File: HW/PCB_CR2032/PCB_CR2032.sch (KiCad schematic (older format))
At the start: 0 parts

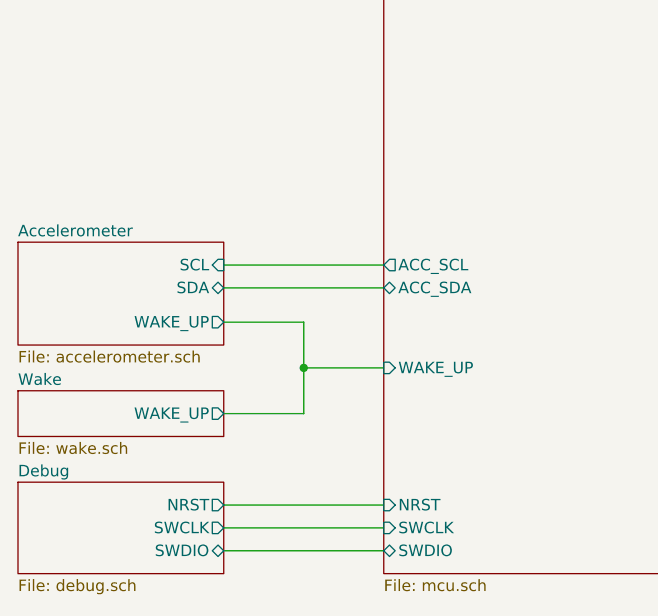
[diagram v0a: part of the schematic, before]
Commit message: * Updated Schematic with 1206 leds and 1k 0805 current limiting resistors
* Restored STDC14 and debug UART, now shared with top led of minute and second. Some other LED pins remapped

* Updated STM32CubeMX project to reflect schematic changes and generated code again
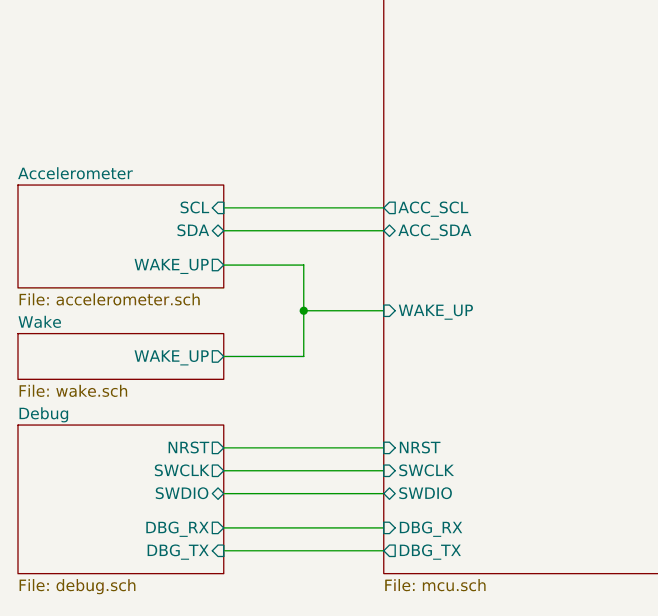
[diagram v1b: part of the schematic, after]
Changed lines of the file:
@@
 Sheet 1 7
 Title "BCD Watch"
-Date "2019-11-06"
-Rev "0.1"
+Date "2019-11-08"
+Rev "0.3"
 Comp ""
 Comment1 ""
@@
 $EndSheet
 $Sheet
-S 2550 4850 900  400
+S 2550 4600 900  650
 U 5DD47181
 F0 "Debug" 50
 F1 "debug.sch" 50
-F2 "NRST" O R 3450 4950 50
-F3 "SWCLK" O R 3450 5050 50
-F4 "SWDIO" B R 3450 5150 50
-$EndSheet
-$Sheet
-S 2550 4450 900  200
+F2 "NRST" O R 3450 4700 50
+F3 "SWCLK" O R 3450 4800 50
+F4 "SWDIO" B R 3450 4900 50
+F5 "DBG_RX" O R 3450 5050 50
+F6 "DBG_TX" I R 3450 5150 50
+$EndSheet
+$Sheet
+S 2550 4200 900  200
 U 5DD502F6
 F0 "Wake" 50
 F1 "wake.sch" 50
-F2 "WAKE_UP" O R 3450 4550 50
-$EndSheet
-Wire Wire Line
-	3450 4950 4150 4950
-Wire Wire Line
-	3450 5050 4150 5050
-Wire Wire Line
-	3450 5150 4150 5150
-$Sheet
-S 2550 3800 900  450
+F2 "WAKE_UP" O R 3450 4300 50
+$EndSheet
+$Sheet
+S 2550 3550 900  450
 U 5DC486A4
 F0 "Accelerometer" 50
 F1 "accelerometer.sch" 50
-F2 "SCL" I R 3450 3900 50
-F3 "SDA" B R 3450 4000 50
-F4 "WAKE_UP" O R 3450 4150 50
-$EndSheet
-Wire Wire Line
-	3450 4150 3800 4150
-Wire Wire Line
-	3800 4150 3800 4350
-Wire Wire Line
-	3800 4350 4150 4350
-Wire Wire Line
-	3450 4550 3800 4550
-Wire Wire Line
-	3800 4550 3800 4350
-Connection ~ 3800 4350
+F2 "SCL" I R 3450 3650 50
+F3 "SDA" B R 3450 3750 50
+F4 "WAKE_UP" O R 3450 3900 50
+$EndSheet
+Wire Wire Line
+	3450 3900 3800 3900
+Wire Wire Line
+	3800 3900 3800 4100
+Wire Wire Line
+	3800 4100 4150 4100
+Wire Wire Line
+	3450 4300 3800 4300
+Wire Wire Line
+	3800 4300 3800 4100
+Connection ~ 3800 4100
 $Sheet
 S 2550 2000 900  400
@@
 F20 "LED_S_01" O R 6400 4250 50
 F21 "LED_S_00" O R 6400 4350 50
-F22 "SWCLK" I L 4150 5050 50
-F23 "SWDIO" B L 4150 5150 50
-F24 "NRST" I L 4150 4950 50
-F25 "WAKE_UP" I L 4150 4350 50
+F22 "SWCLK" I L 4150 4800 50
+F23 "SWDIO" B L 4150 4900 50
+F24 "NRST" I L 4150 4700 50
+F25 "WAKE_UP" I L 4150 4100 50
 F26 "LED_H_1_DIM" O R 6400 4550 50
 F27 "LED_H_0_DIM" O R 6400 4650 50
@@
 F34 "LED_M_13" O R 6400 2650 50
 F35 "LED_S_13" O R 6400 3600 50
-F36 "ACC_SDA" B L 4150 4000 50
-F37 "ACC_SCL" O L 4150 3900 50
-$EndSheet
-Wire Wire Line
-	3450 3900 4150 3900
-Wire Wire Line
-	3450 4000 4150 4000
+F36 "ACC_SDA" B L 4150 3750 50
+F37 "ACC_SCL" O L 4150 3650 50
+F38 "DBG_TX" O L 4150 5150 50
+F39 "DBG_RX" I L 4150 5050 50
+$EndSheet
+Wire Wire Line
+	3450 3650 4150 3650
+Wire Wire Line
+	3450 3750 4150 3750
 Wire Wire Line
 	6400 5150 7100 5150
@@
 Wire Wire Line
 	6400 1700 7100 1700
+Wire Wire Line
+	4150 4700 3450 4700
+Wire Wire Line
+	3450 4800 4150 4800
+Wire Wire Line
+	3450 4900 4150 4900
+Wire Wire Line
+	3450 5050 4150 5050
+Wire Wire Line
+	3450 5150 4150 5150
 $EndSCHEMATC

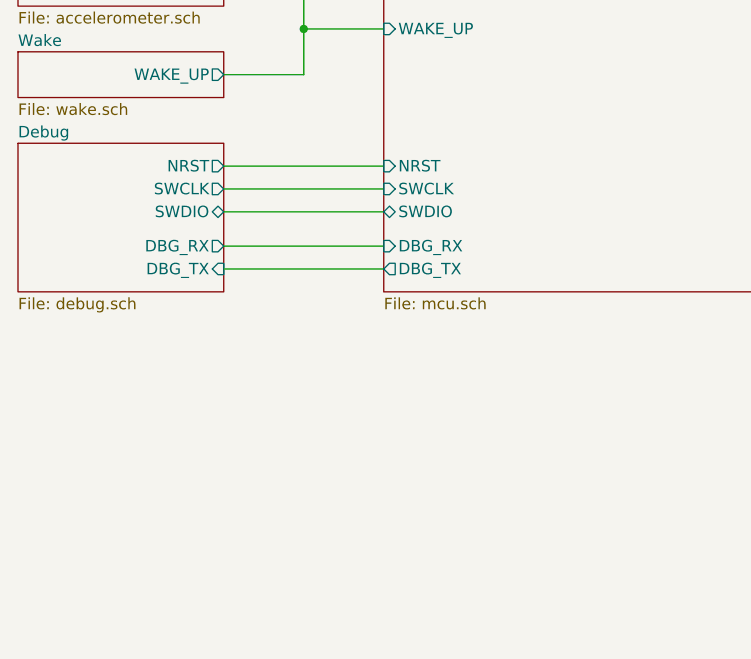
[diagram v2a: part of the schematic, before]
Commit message: Worked on Rev 2.0 HW with smaller size.
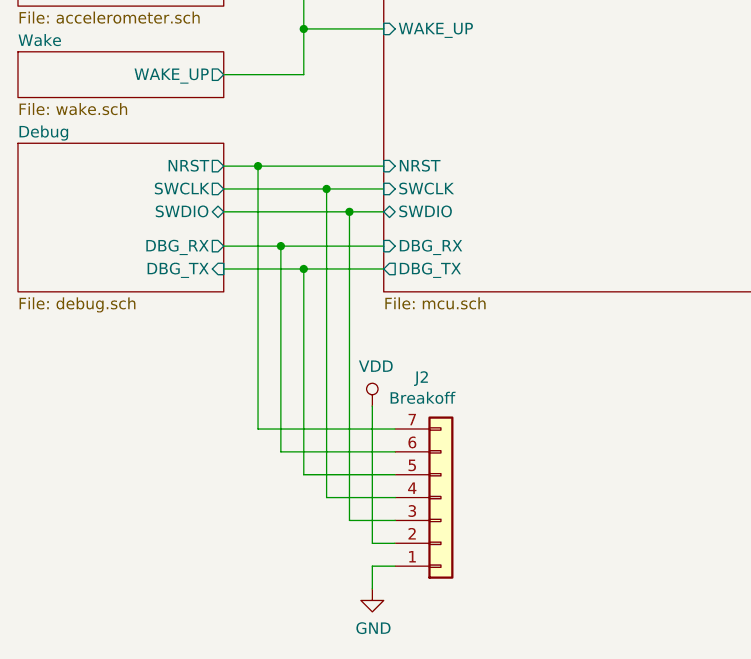
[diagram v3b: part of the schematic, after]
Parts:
- added J2: Breakoff, Connector_PinHeader_1.27mm:PinHeader_1x07_P1.27mm_Vertical, symbol Connector_Generic:Conn_01x07
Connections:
- net Debug/DBG_RX: now also J2.6 (Pin_6)
- net Debug/DBG_TX: now also J2.5 (Pin_5)
- net Debug/NRST: now also J2.7 (Pin_7)
- net Debug/SWCLK: now also J2.4 (Pin_4)
- net Debug/SWDIO: now also J2.3 (Pin_3)
- new net GND: J2.1 (Pin_1)
- new net VDD: J2.2 (Pin_2)
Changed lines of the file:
@@
 Wire Wire Line
 	6400 1700 7100 1700
+$Comp
+L Connector_Generic:Conn_01x07 J2
+U 1 1 5DCC8438
+P 4400 6150
+F 0 "J2" H 4318 5625 50  0000 C CNN
+F 1 "Breakoff" H 4318 5716 50  0000 C CNN
+F 2 "Connector_PinHeader_1.27mm:PinHeader_1x07_P1.27mm_Vertical" H 4400 6150 50  0001 C CNN
+F 3 "~" H 4400 6150 50  0001 C CNN
+	1    4400 6150
+	1    0    0    1
+$EndComp
+$Comp
+L power:GND #PWR017
+U 1 1 5DCCDE70
+P 4100 6550
+F 0 "#PWR017" H 4100 6300 50  0001 C CNN
+F 1 "GND" H 4105 6377 50  0000 C CNN
+F 2 "" H 4100 6550 50  0001 C CNN
+F 3 "" H 4100 6550 50  0001 C CNN
+	1    4100 6550
+	1    0    0    -1
+$EndComp
 Wire Wire Line
-	4150 4700 3450 4700
+	4100 6450 4100 6550
 Wire Wire Line
-	3450 4800 4150 4800
+	4100 6450 4200 6450
+$Comp
+L power:VDD #PWR0101
+U 1 1 5DCE07CE
+P 4100 5750
+F 0 "#PWR0101" H 4100 5600 50  0001 C CNN
+F 1 "VDD" H 4117 5923 50  0000 C CNN
+F 2 "" H 4100 5750 50  0001 C CNN
+F 3 "" H 4100 5750 50  0001 C CNN
+	1    4100 5750
+	1    0    0    -1
+$EndComp
 Wire Wire Line
-	3450 4900 4150 4900
+	4200 6350 4100 6350
 Wire Wire Line
-	3450 5050 4150 5050
+	4100 5750 4100 6350
 Wire Wire Line
-	3450 5150 4150 5150
+	3450 4700 3600 4700
+Wire Wire Line
+	4200 5850 3600 5850
+Wire Wire Line
+	3600 5850 3600 4700
+Connection ~ 3600 4700
+Wire Wire Line
+	3450 5050 3700 5050
+Wire Wire Line
+	4000 4900 4150 4900
+Connection ~ 4000 4900
+Wire Wire Line
+	4000 6250 4000 4900
+Wire Wire Line
+	4200 6250 4000 6250
+Wire Wire Line
+	3450 4900 4000 4900
+Wire Wire Line
+	4200 6150 3900 6150
+Wire Wire Line
+	3900 6150 3900 4800
+Connection ~ 3900 4800
+Wire Wire Line
+	3900 4800 4150 4800
+Wire Wire Line
+	3450 4800 3900 4800
+Wire Wire Line
+	3600 4700 4150 4700
+Wire Wire Line
+	4200 6050 3800 6050
+Wire Wire Line
+	3800 6050 3800 5150
+Connection ~ 3800 5150
+Wire Wire Line
+	3800 5150 4150 5150
+Wire Wire Line
+	3450 5150 3800 5150
+Wire Wire Line
+	4200 5950 3700 5950
+Wire Wire Line
+	3700 5950 3700 5050
+Connection ~ 3700 5050
+Wire Wire Line
+	3700 5050 4150 5050
 $EndSCHEMATC
